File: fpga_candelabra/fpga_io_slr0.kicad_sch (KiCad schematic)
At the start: 1 part, among them U1 XCVU13P-B2104

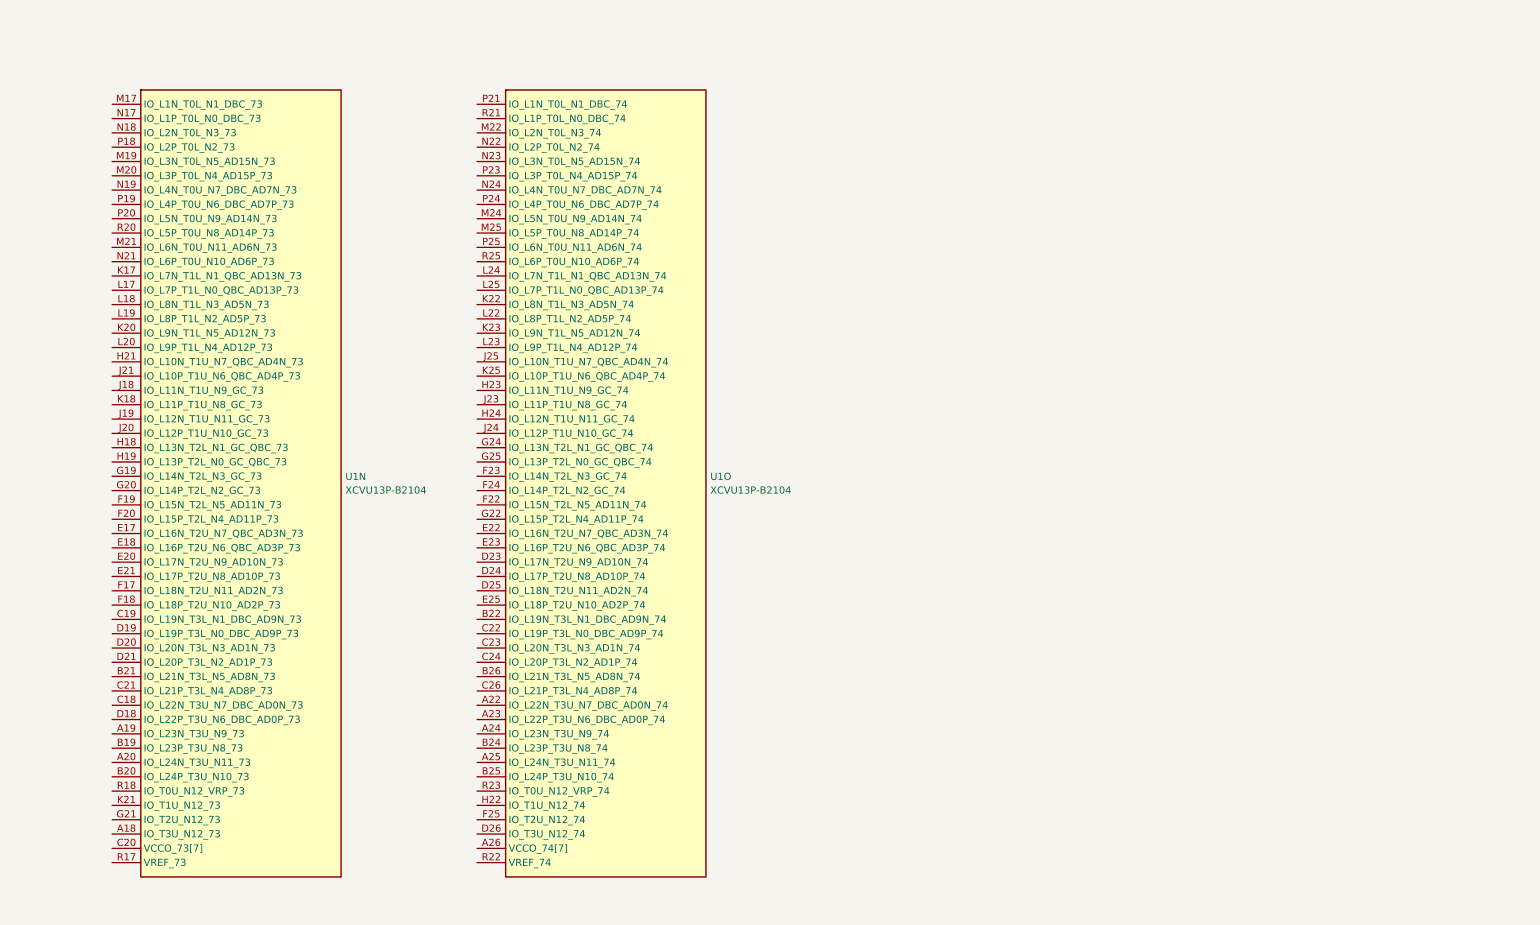
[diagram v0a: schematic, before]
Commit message: fpga_candelabra: reorganize fpga io and mgt by SLR
- Rename sch sheets
- Add prelimary DDR and PCIE Bank/Quad allocation

Signed-off-by: Yichuan Gao <gaoyichuan000@gmail.com>
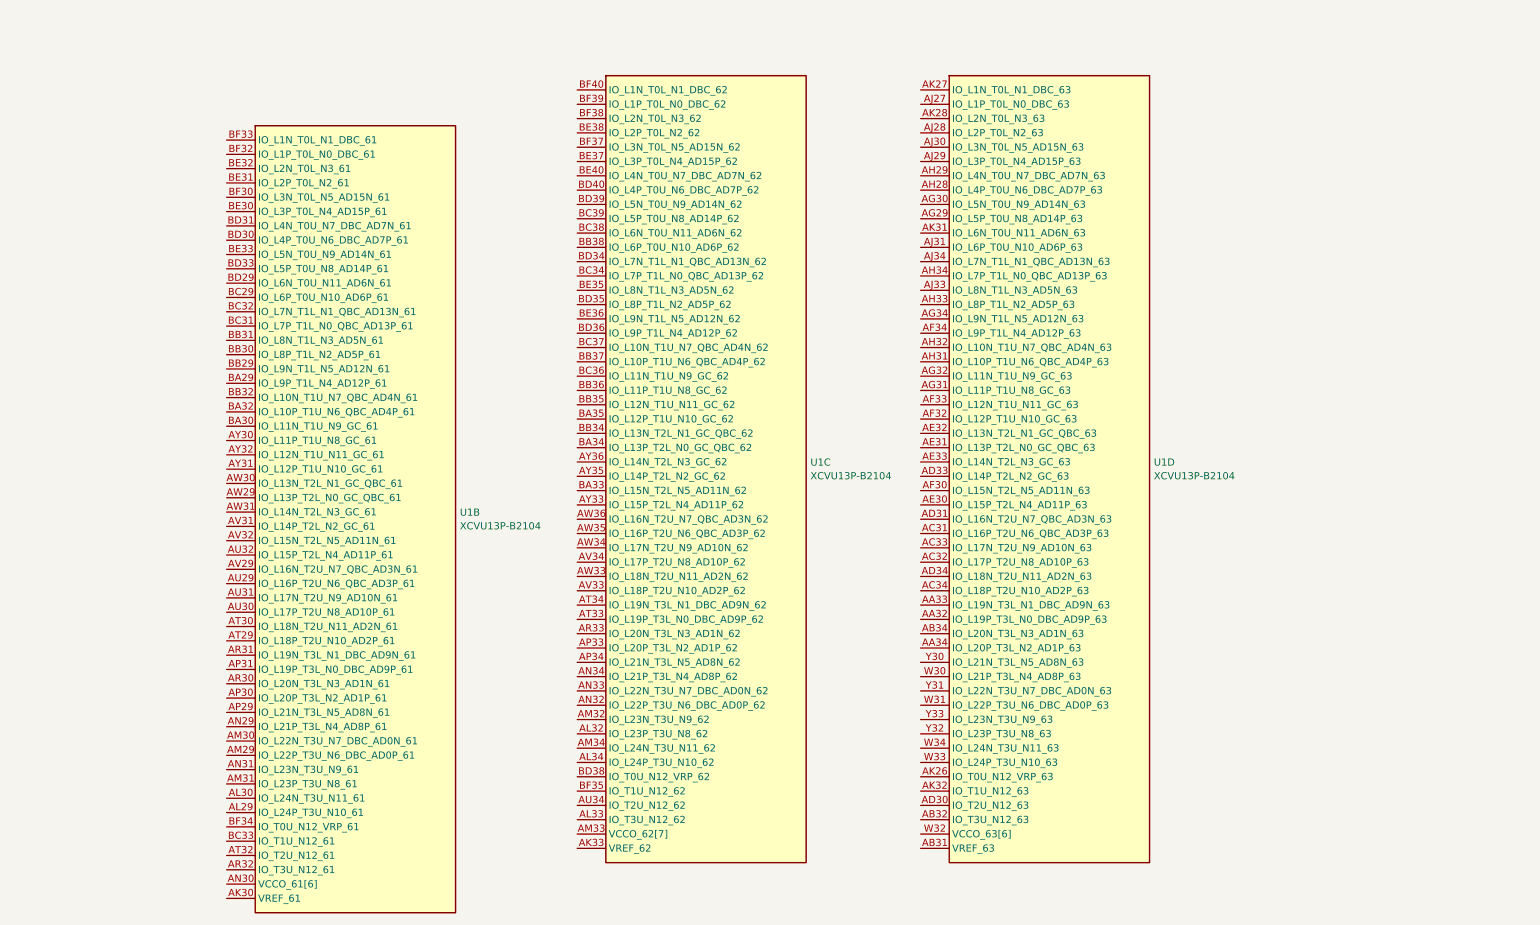
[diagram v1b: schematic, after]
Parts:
- removed U1: XCVU13P-B2104, CHIPSAlliance_Package_BGA:Xilinx_FHGB2104_VU13P_PkgLength, symbol CHIPSAlliance_FPGA_Xilinx_Virtex_UltraScale_Plus:XCVU13P-B2104
- added U1: XCVU13P-B2104, CHIPSAlliance_Package_BGA:Xilinx_FHGB2104_VU13P_PkgLength, symbol CHIPSAlliance_FPGA_Xilinx_Virtex_UltraScale_Plus:XCVU13P-B2104
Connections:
- new net: U1.AB33 (VCCO_63[6]), U1.AE34 (VCCO_63[6]), U1.AF31 (VCCO_63[6]), U1.AJ32 (VCCO_63[6]), U1.AK29 (VCCO_63[6]), U1.W32 (VCCO_63[6])
- new net: U1.AM33 (VCCO_62[7]), U1.AR34 (VCCO_62[7]), U1.BA36 (VCCO_62[7]), U1.BB33 (VCCO_62[7]), U1.BC40 (VCCO_62[7]), U1.BD37 (VCCO_62[7]), U1.BE34 (VCCO_62[7])
- new net: U1.AN30 (VCCO_61[6]), U1.AT31 (VCCO_61[6]), U1.AW32 (VCCO_61[6]), U1.AY29 (VCCO_61[6]), U1.BC30 (VCCO_61[6]), U1.BF31 (VCCO_61[6])

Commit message: candelabra: add i-pex extension ports, remove FMC1
* update bank/mgt allocation
* add basic pcb floorplanning

Signed-off-by: Yichuan Gao <gaoyichuan000@gmail.com>
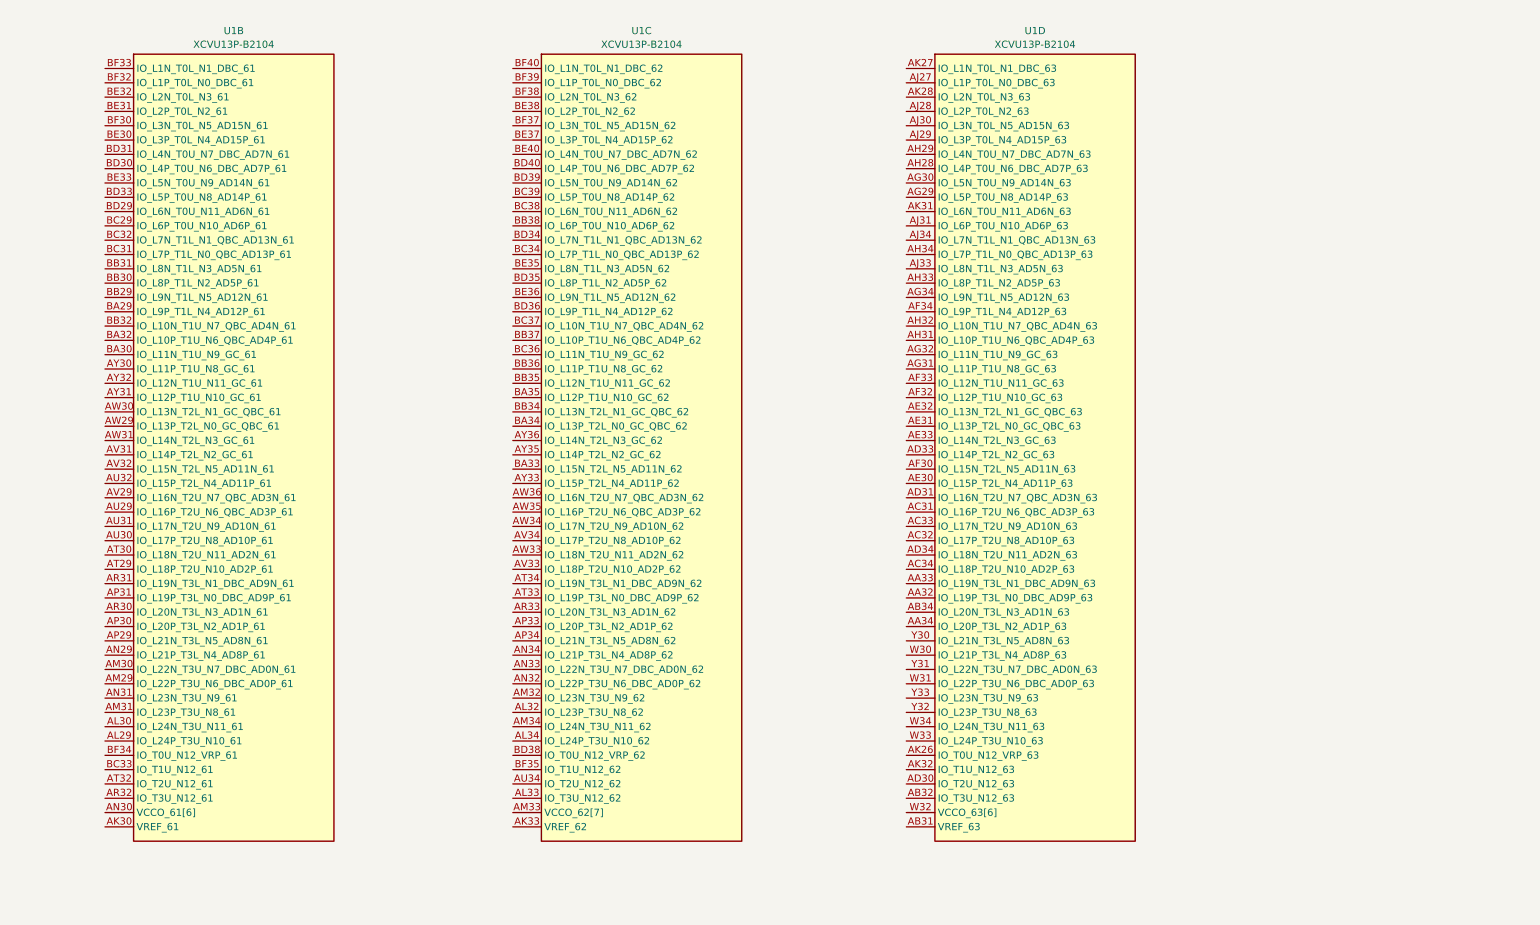
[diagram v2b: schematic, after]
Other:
- moved on the sheet: U1B, U1C, U1D
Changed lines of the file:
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@@
 	(symbol
 		(lib_id "CHIPSAlliance_FPGA_Xilinx_Virtex_UltraScale_Plus:XCVU13P-B2104")
-		(at 175.26 27.94 0)
+		(at 172.72 24.13 0)
 		(unit 4)
 		(exclude_from_sim no)
@@
 		(fields_autoplaced yes)
 		(property "Reference" "U1"
-			(at 216.662 94.0378 0)
+			(at 195.58 17.4455 0)
 			(effects
 				(font
 					(size 1.27 1.27)
 				)
-				(justify left)
 			)
 		)
 		(property "Value" "XCVU13P-B2104"
-			(at 216.662 96.4621 0)
+			(at 195.58 19.8698 0)
 			(effects
 				(font
 					(size 1.27 1.27)
 				)
-				(justify left)
 			)
 		)
 		(property "Footprint" "CHIPSAlliance_Package_BGA:Xilinx_FHGB2104_VU13P_PkgLength"
-			(at 173.99 26.67 0)
+			(at 171.45 22.86 0)
 			(effects
 				(font
@@
 		)
 		(property "Datasheet" ""
-			(at 173.99 64.77 0)
+			(at 171.45 60.96 0)
 			(effects
 				(font
@@
 		)
 		(property "Description" "Virtex UltraScale+ 13P XCVU13P-B2104"
-			(at 175.26 27.94 0)
+			(at 172.72 24.13 0)
 			(effects
 				(font
@@
 	(symbol
 		(lib_id "CHIPSAlliance_FPGA_Xilinx_Virtex_UltraScale_Plus:XCVU13P-B2104")
-		(at 114.3 27.94 0)
+		(at 102.87 24.13 0)
 		(unit 3)
 		(exclude_from_sim no)
@@
 		(fields_autoplaced yes)
 		(property "Reference" "U1"
-			(at 155.702 94.0378 0)
+			(at 125.73 17.4455 0)
 			(effects
 				(font
 					(size 1.27 1.27)
 				)
-				(justify left)
 			)
 		)
 		(property "Value" "XCVU13P-B2104"
-			(at 155.702 96.4621 0)
+			(at 125.73 19.8698 0)
 			(effects
 				(font
 					(size 1.27 1.27)
 				)
-				(justify left)
 			)
 		)
 		(property "Footprint" "CHIPSAlliance_Package_BGA:Xilinx_FHGB2104_VU13P_PkgLength"
-			(at 113.03 26.67 0)
+			(at 101.6 22.86 0)
 			(effects
 				(font
@@
 		)
 		(property "Datasheet" ""
-			(at 113.03 64.77 0)
+			(at 101.6 60.96 0)
 			(effects
 				(font
@@
 		)
 		(property "Description" "Virtex UltraScale+ 13P XCVU13P-B2104"
-			(at 114.3 27.94 0)
+			(at 102.87 24.13 0)
 			(effects
 				(font
@@
 	(symbol
 		(lib_id "CHIPSAlliance_FPGA_Xilinx_Virtex_UltraScale_Plus:XCVU13P-B2104")
-		(at 52.07 36.83 0)
+		(at 30.48 24.13 0)
 		(unit 2)
 		(exclude_from_sim no)
@@
 		(fields_autoplaced yes)
 		(property "Reference" "U1"
-			(at 93.472 102.9278 0)
+			(at 53.34 17.4455 0)
 			(effects
 				(font
 					(size 1.27 1.27)
 				)
-				(justify left)
 			)
 		)
 		(property "Value" "XCVU13P-B2104"
-			(at 93.472 105.3521 0)
+			(at 53.34 19.8698 0)
 			(effects
 				(font
 					(size 1.27 1.27)
 				)
-				(justify left)
 			)
 		)
 		(property "Footprint" "CHIPSAlliance_Package_BGA:Xilinx_FHGB2104_VU13P_PkgLength"
-			(at 50.8 35.56 0)
+			(at 29.21 22.86 0)
 			(effects
 				(font
@@
 		)
 		(property "Datasheet" ""
-			(at 50.8 73.66 0)
+			(at 29.21 60.96 0)
 			(effects
 				(font
@@
 		)
 		(property "Description" "Virtex UltraScale+ 13P XCVU13P-B2104"
-			(at 52.07 36.83 0)
+			(at 30.48 24.13 0)
 			(effects
 				(font

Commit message: fpga_candelabra: major revision
* Finish DDR4 & QSFP+ & PCIe layout
* Change FMC to LPC
* Add mikroBUS extension
* 12V input & PDN updates
* FPGA config updates

Signed-off-by: Yichuan Gao <gaoyichuan000@gmail.com>
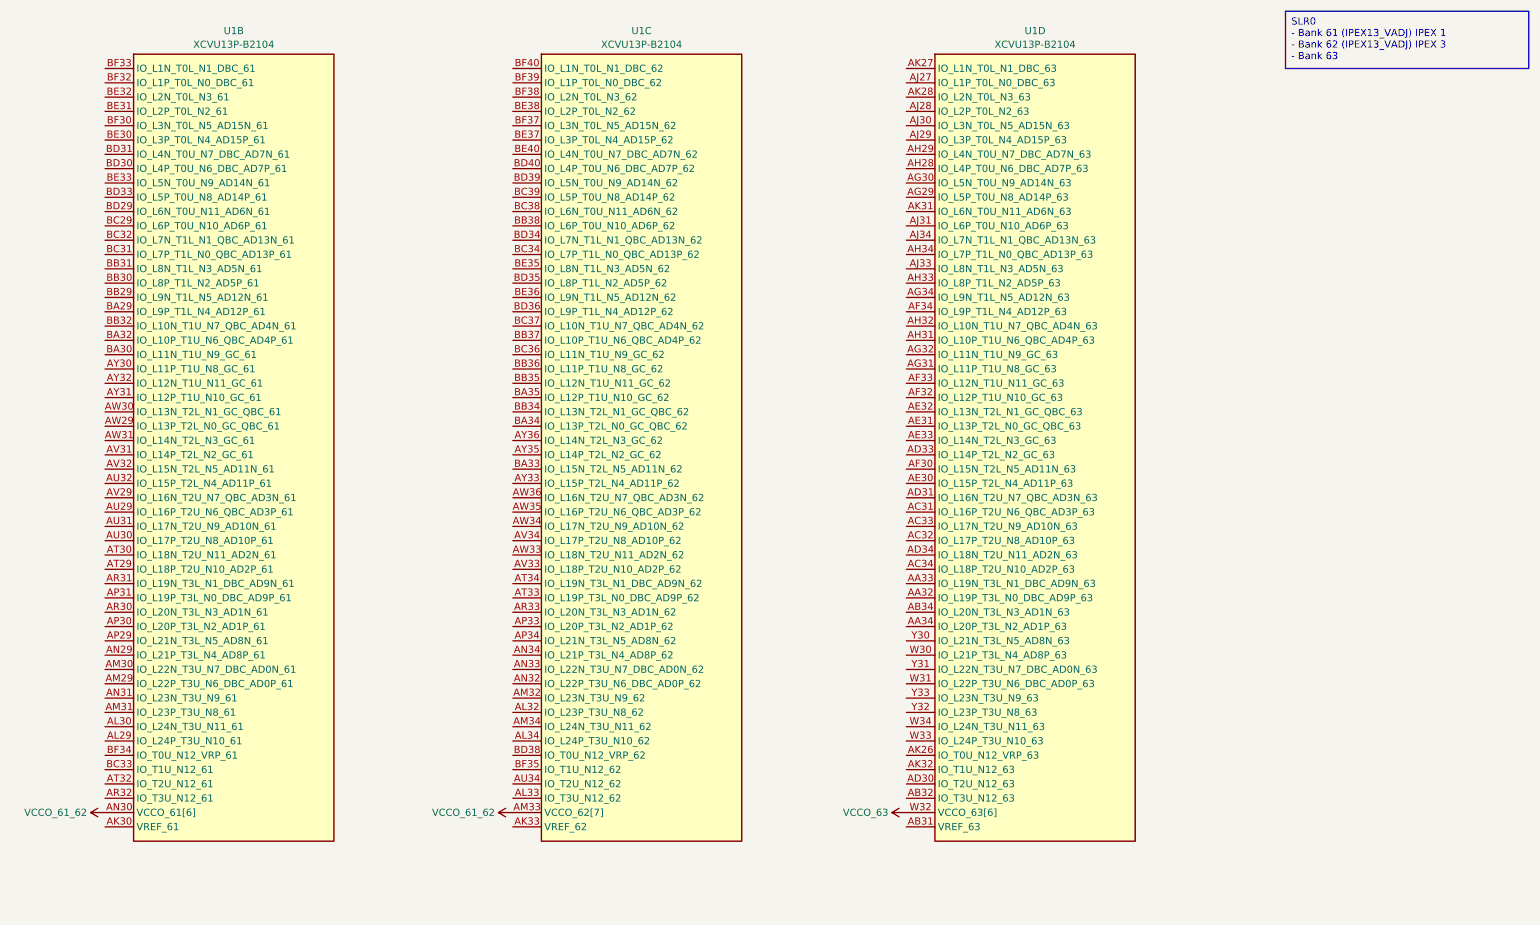
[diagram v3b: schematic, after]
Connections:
- net VCCO_63: now reaches U1.AB33 (VCCO_63[6]), U1.AE34 (VCCO_63[6]), U1.AF31 (VCCO_63[6]), U1.AJ32 (VCCO_63[6]), U1.AK29 (VCCO_63[6]), U1.W32 (VCCO_63[6])
- net VCCO_61_62: now reaches U1.AM33 (VCCO_62[7]), U1.AR34 (VCCO_62[7]), U1.BA36 (VCCO_62[7]), U1.BB33 (VCCO_62[7]), U1.BC40 (VCCO_62[7]), U1.BD37 (VCCO_62[7]), U1.BE34 (VCCO_62[7])
- net VCCO_61_62: now also U1.AN30 (VCCO_61[6]), U1.AT31 (VCCO_61[6]), U1.AW32 (VCCO_61[6]), U1.AY29 (VCCO_61[6]), U1.BC30 (VCCO_61[6]), U1.BF31 (VCCO_61[6])
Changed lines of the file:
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@@
 	(generator_version "8.0")
 	(paper "A4")
+	(text_box "SLR0\n  - Bank 61 (IPEX13_VADJ) IPEX 1\n  - Bank 62 (IPEX13_VADJ) IPEX 3\n  - Bank 63"
+		(exclude_from_sim no)
+		(at 240.03 13.97 0)
+		(size 43.18 10.16)
+		(stroke
+			(width 0)
+			(type default)
+		)
+		(fill
+			(type none)
+		)
+		(effects
+			(font
+				(size 1.27 1.27)
+			)
+			(justify left top)
+		)
+	)
+	(symbol
+		(lib_id "power:+12V")
+		(at 30.48 156.21 90)
+		(unit 1)
+		(exclude_from_sim no)
+		(in_bom yes)
+		(on_board yes)
+		(dnp no)
+		(fields_autoplaced yes)
+		(property "Reference" "#PWR0504"
+			(at 34.29 156.21 0)
+			(effects
+				(font
+					(size 1.27 1.27)
+				)
+				(hide yes)
+			)
+		)
+		(property "Value" "VCCO_61_62"
+			(at 27.3051 156.21 90)
+			(effects
+				(font
+					(size 1.27 1.27)
+				)
+				(justify left)
+			)
+		)
+		(property "Footprint" ""
+			(at 30.48 156.21 0)
+			(effects
+				(font
+					(size 1.27 1.27)
+				)
+				(hide yes)
+			)
+		)
+		(property "Datasheet" ""
+			(at 30.48 156.21 0)
+			(effects
+				(font
+					(size 1.27 1.27)
+				)
+				(hide yes)
+			)
+		)
+		(property "Description" "Power symbol creates a global label with name \"+12V\""
+			(at 30.48 156.21 0)
+			(effects
+				(font
+					(size 1.27 1.27)
+				)
+				(hide yes)
+			)
+		)
+		(pin "1"
+		)
+		(instances
+			(project "fpga_candelabra"
+				(path "/01ed9e92-4e50-4b41-90dc-10444aaec5f7/7068e078-a22b-4ea0-8b1f-88b1ba691cbb"
+					(reference "#PWR0504")
+					(unit 1)
+				)
+			)
+		)
+	)
+	(symbol
+		(lib_id "power:+12V")
+		(at 172.72 156.21 90)
+		(unit 1)
+		(exclude_from_sim no)
+		(in_bom yes)
+		(on_board yes)
+		(dnp no)
+		(fields_autoplaced yes)
+		(property "Reference" "#PWR0316"
+			(at 176.53 156.21 0)
+			(effects
+				(font
+					(size 1.27 1.27)
+				)
+				(hide yes)
+			)
+		)
+		(property "Value" "VCCO_63"
+			(at 169.5451 156.21 90)
+			(effects
+				(font
+					(size 1.27 1.27)
+				)
+				(justify left)
+			)
+		)
+		(property "Footprint" ""
+			(at 172.72 156.21 0)
+			(effects
+				(font
+					(size 1.27 1.27)
+				)
+				(hide yes)
+			)
+		)
+		(property "Datasheet" ""
+			(at 172.72 156.21 0)
+			(effects
+				(font
+					(size 1.27 1.27)
+				)
+				(hide yes)
+			)
+		)
+		(property "Description" "Power symbol creates a global label with name \"+12V\""
+			(at 172.72 156.21 0)
+			(effects
+				(font
+					(size 1.27 1.27)
+				)
+				(hide yes)
+			)
+		)
+		(pin "1"
+		)
+		(instances
+			(project "fpga_candelabra"
+				(path "/01ed9e92-4e50-4b41-90dc-10444aaec5f7/7068e078-a22b-4ea0-8b1f-88b1ba691cbb"
+					(reference "#PWR0316")
+					(unit 1)
+				)
+			)
+		)
+	)
+	(symbol
+		(lib_id "power:+12V")
+		(at 102.87 156.21 90)
+		(unit 1)
+		(exclude_from_sim no)
+		(in_bom yes)
+		(on_board yes)
+		(dnp no)
+		(fields_autoplaced yes)
+		(property "Reference" "#PWR0164"
+			(at 106.68 156.21 0)
+			(effects
+				(font
+					(size 1.27 1.27)
+				)
+				(hide yes)
+			)
+		)
+		(property "Value" "VCCO_61_62"
+			(at 99.6951 156.21 90)
+			(effects
+				(font
+					(size 1.27 1.27)
+				)
+				(justify left)
+			)
+		)
+		(property "Footprint" ""
+			(at 102.87 156.21 0)
+			(effects
+				(font
+					(size 1.27 1.27)
+				)
+				(hide yes)
+			)
+		)
+		(property "Datasheet" ""
+			(at 102.87 156.21 0)
+			(effects
+				(font
+					(size 1.27 1.27)
+				)
+				(hide yes)
+			)
+		)
+		(property "Description" "Power symbol creates a global label with name \"+12V\""
+			(at 102.87 156.21 0)
+			(effects
+				(font
+					(size 1.27 1.27)
+				)
+				(hide yes)
+			)
+		)
+		(pin "1"
+		)
+		(instances
+			(project "fpga_candelabra"
+				(path "/01ed9e92-4e50-4b41-90dc-10444aaec5f7/7068e078-a22b-4ea0-8b1f-88b1ba691cbb"
+					(reference "#PWR0164")
+					(unit 1)
+				)
+			)
+		)
+	)
 	(symbol
 		(lib_id "CHIPSAlliance_FPGA_Xilinx_Virtex_UltraScale_Plus:XCVU13P-B2104")
